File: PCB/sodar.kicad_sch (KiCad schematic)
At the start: 70 parts, among them J1 Screw_Terminal_01x02, J2 Conn_02x12_Counter_Clockwise, J3 Conn_01x02, U1 TC78H621FNG, U10 TC78H621FNG, U2 TC78H621FNG, U3 TC78H621FNG, U4 TC78H621FNG, U5 TC78H621FNG, U6 TC78H621FNG, U7 TC78H621FNG, U8 TC78H621FNG, U9 TC78H621FNG

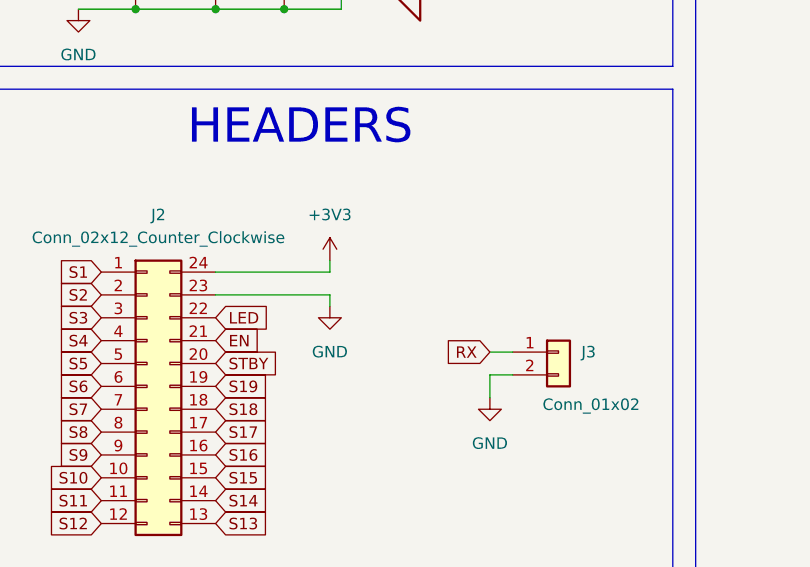
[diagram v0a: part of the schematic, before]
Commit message: Added a bulk cap on 3V3 line
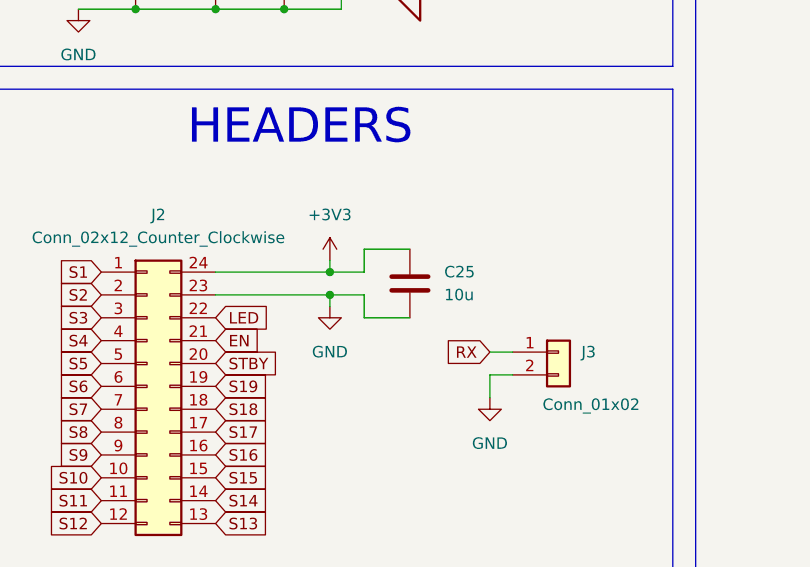
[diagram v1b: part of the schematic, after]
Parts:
- added C25: 10u, Capacitor_SMD:C_0805_2012Metric, symbol Device:C
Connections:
- net +3V3: now also C25.1
- net GND: now also C25.2
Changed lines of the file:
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@@
 	)
 	(junction
+		(at 217.17 66.04)
+		(diameter 0)
+		(color 0 0 0 0)
+	)
+	(junction
 		(at 347.98 76.2)
 		(diameter 0)
@@
 	)
 	(junction
+		(at 217.17 63.5)
+		(diameter 0)
+		(color 0 0 0 0)
+	)
+	(junction
 		(at 140.97 138.43)
 		(diameter 0)
@@
 	(wire
 		(pts
+			(xy 220.98 68.58) (xy 226.06 68.58)
+		)
+		(stroke
+			(width 0)
+			(type default)
+		)
+	)
+	(wire
+		(pts
 			(xy 104.14 66.04) (xy 104.14 67.31)
 		)
@@
 	(wire
 		(pts
+			(xy 220.98 63.5) (xy 217.17 63.5)
+		)
+		(stroke
+			(width 0)
+			(type default)
+		)
+	)
+	(wire
+		(pts
 			(xy 130.81 147.32) (xy 135.89 147.32)
 		)
@@
 	(wire
 		(pts
+			(xy 220.98 60.96) (xy 220.98 63.5)
+		)
+		(stroke
+			(width 0)
+			(type default)
+		)
+	)
+	(wire
+		(pts
 			(xy 29.21 175.26) (xy 30.48 175.26)
 		)
@@
 	(wire
 		(pts
+			(xy 220.98 66.04) (xy 220.98 68.58)
+		)
+		(stroke
+			(width 0)
+			(type default)
+		)
+	)
+	(wire
+		(pts
 			(xy 140.97 96.52) (xy 140.97 104.14)
 		)
@@
 	(wire
 		(pts
+			(xy 226.06 60.96) (xy 220.98 60.96)
+		)
+		(stroke
+			(width 0)
+			(type default)
+		)
+	)
+	(wire
+		(pts
 			(xy 240.03 124.46) (xy 240.03 121.92)
 		)
@@
 	(wire
 		(pts
+			(xy 217.17 66.04) (xy 220.98 66.04)
+		)
+		(stroke
+			(width 0)
+			(type default)
+		)
+	)
+	(wire
+		(pts
 			(xy 285.75 41.91) (xy 285.75 45.72)
 		)
@@
 					(unit 1)
 				)
+			)
+		)
+	)
+	(symbol
+		(lib_id "Device:C")
+		(at 226.06 64.77 0)
+		(unit 1)
+		(exclude_from_sim no)
+		(in_bom yes)
+		(on_board yes)
+		(dnp no)
+		(fields_autoplaced yes)
+		(property "Reference" "C25"
+			(at 229.87 63.4999 0)
+			(effects
+				(font
+					(size 1.27 1.27)
+				)
+				(justify left)
+			)
+		)
+		(property "Value" "10u"
+			(at 229.87 66.0399 0)
+			(effects
+				(font
+					(size 1.27 1.27)
+				)
+				(justify left)
+			)
+		)
+		(property "Footprint" "Capacitor_SMD:C_0805_2012Metric"
+			(at 227.0252 68.58 0)
+			(effects
+				(font
+					(size 1.27 1.27)
+				)
+				(hide yes)
+			)
+		)
+		(property "Datasheet" "~"
+			(at 226.06 64.77 0)
+			(effects
+				(font
+					(size 1.27 1.27)
+				)
+				(hide yes)
+			)
+		)
+		(property "Description" "Unpolarized capacitor"
+			(at 226.06 64.77 0)
+			(effects
+				(font
+					(size 1.27 1.27)
+				)
+				(hide yes)
+			)
+		)
+		(pin "2"
+		)
+		(pin "1"
+		)
+		(instances
+			(project ""
+				(path "/f620949f-55f1-4ffa-a6f4-2a6276be8919"
+					(reference "C25")
+					(unit 1)
+				)

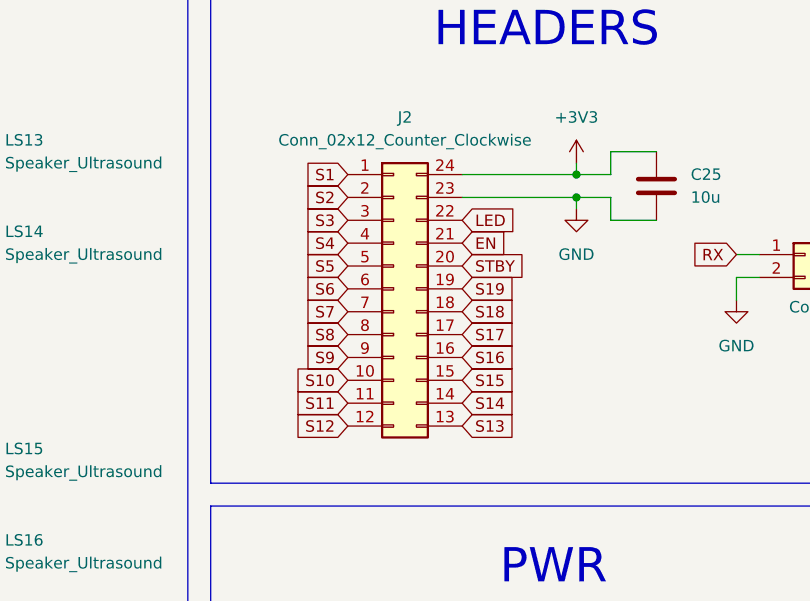
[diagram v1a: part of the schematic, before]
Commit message: Moved signal connections on the header for easier routing
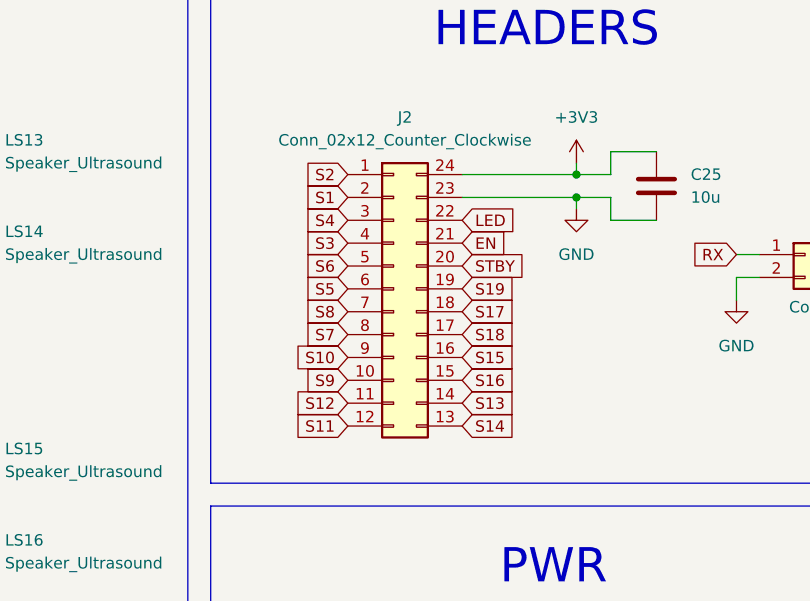
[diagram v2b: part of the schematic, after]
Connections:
- net S1: now also J2.2 (Pin_2); no longer J2.1 (Pin_1)
- net S10: now also J2.9 (Pin_9); no longer J2.10 (Pin_10)
- net S11: now also J2.12 (Pin_12); no longer J2.11 (Pin_11)
- net S12: now also J2.11 (Pin_11); no longer J2.12 (Pin_12)
- net S13: now also J2.14 (Pin_14); no longer J2.13 (Pin_13)
- net S14: now also J2.13 (Pin_13); no longer J2.14 (Pin_14)
- net S15: now also J2.16 (Pin_16); no longer J2.15 (Pin_15)
- net S16: now also J2.15 (Pin_15); no longer J2.16 (Pin_16)
- net S17: now also J2.18 (Pin_18); no longer J2.17 (Pin_17)
- net S18: now also J2.17 (Pin_17); no longer J2.18 (Pin_18)
- net S2: now also J2.1 (Pin_1); no longer J2.2 (Pin_2)
- net S3: now also J2.4 (Pin_4); no longer J2.3 (Pin_3)
- net S4: now also J2.3 (Pin_3); no longer J2.4 (Pin_4)
- net S5: now also J2.6 (Pin_6); no longer J2.5 (Pin_5)
- net S6: now also J2.5 (Pin_5); no longer J2.6 (Pin_6)
- net S7: now also J2.8 (Pin_8); no longer J2.7 (Pin_7)
- net S8: now also J2.7 (Pin_7); no longer J2.8 (Pin_8)
- net S9: now also J2.10 (Pin_10); no longer J2.9 (Pin_9)

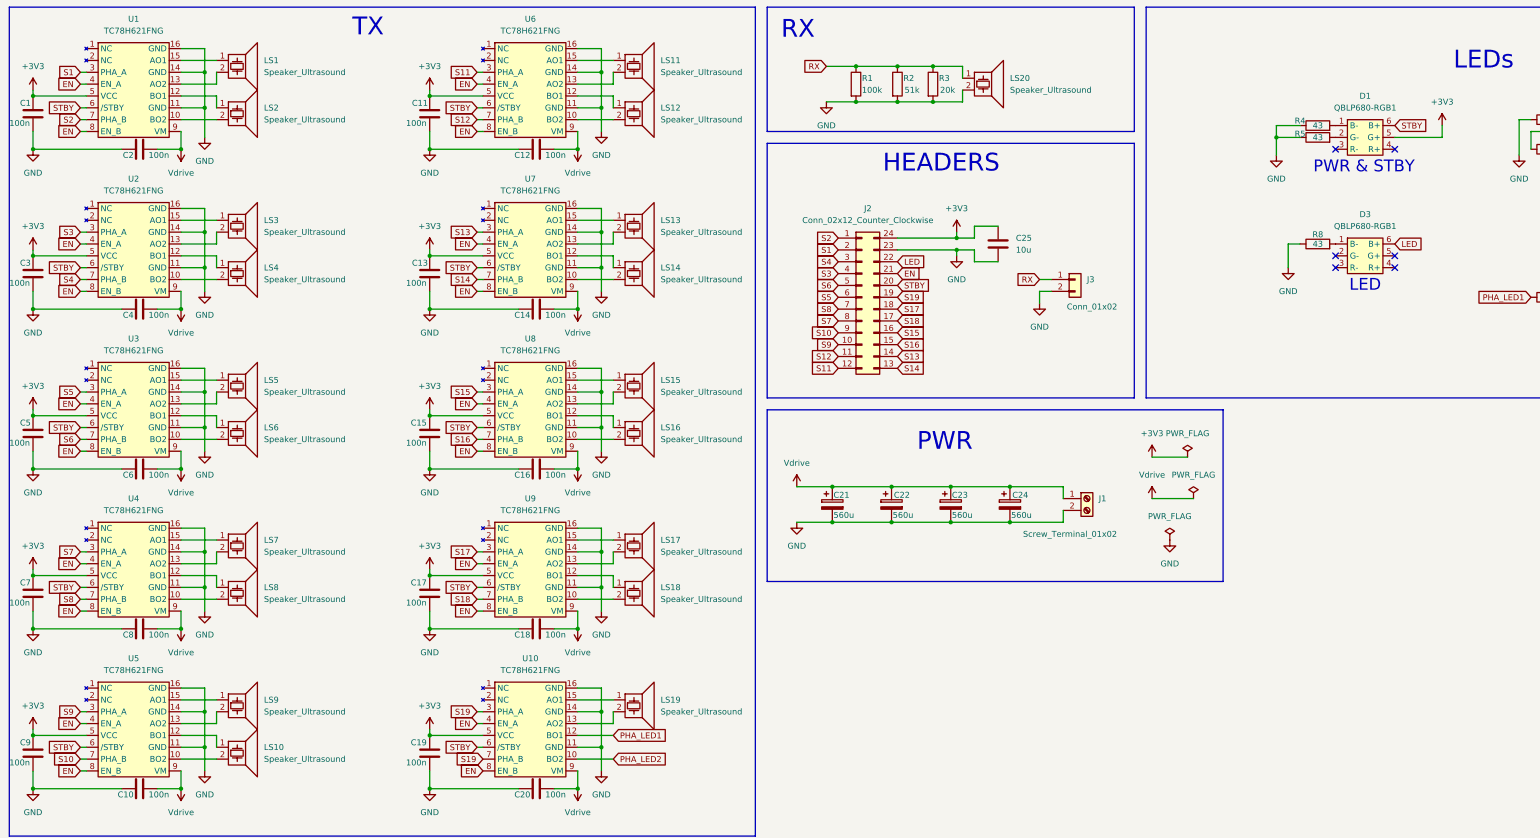
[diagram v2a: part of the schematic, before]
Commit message: Rerouted STBY to 3V3 as we set it to 3V3 anyway
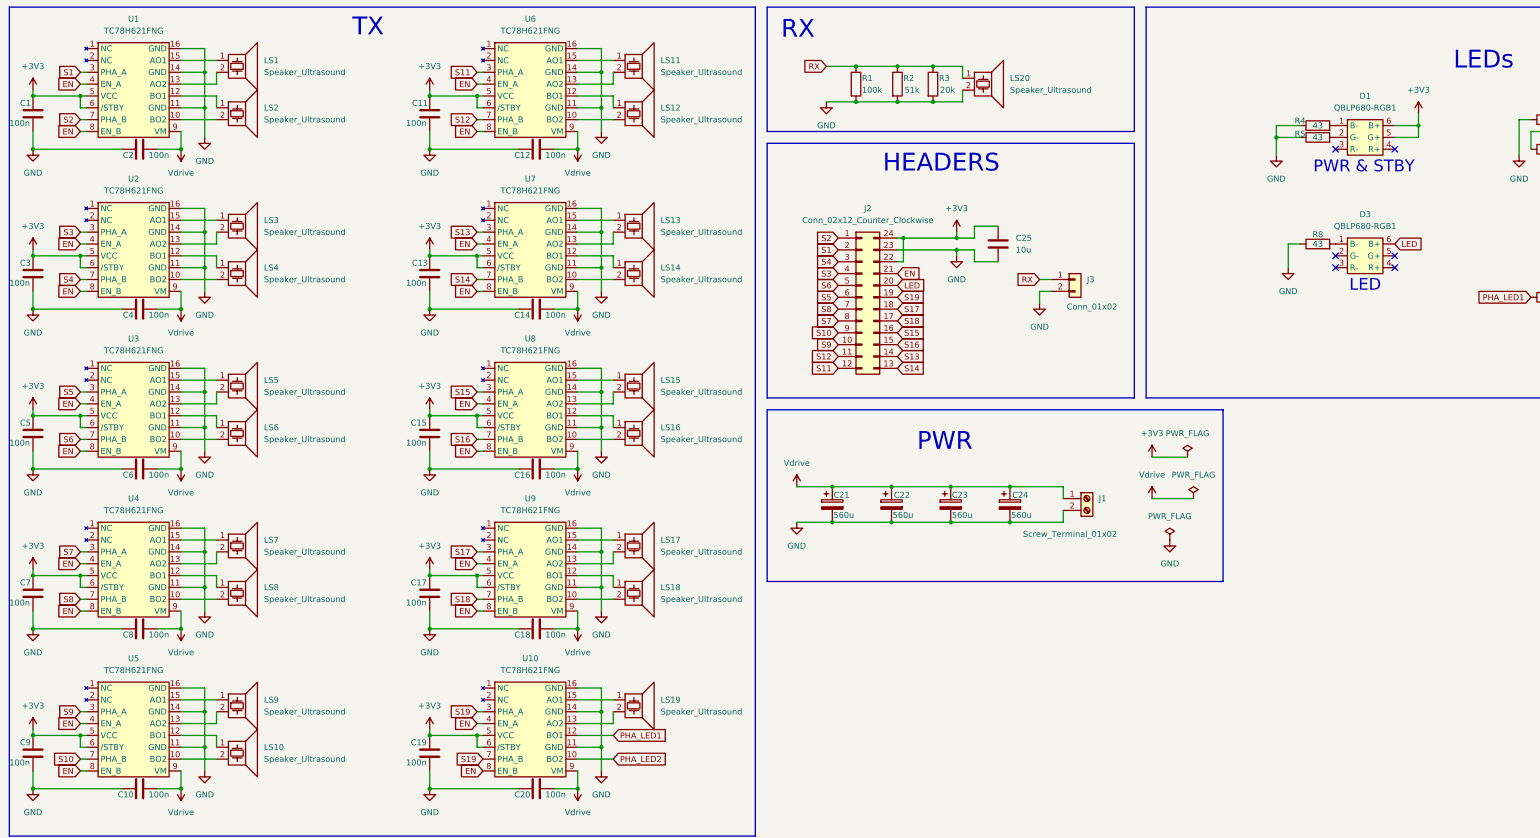
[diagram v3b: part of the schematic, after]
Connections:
- net +3V3: now also D1.6 (B+), J2.22 (Pin_22), U1.6 (/STBY), U10.6 (/STBY), U2.6 (/STBY), U3.6 (/STBY), U4.6 (/STBY), U5.6 (/STBY), U6.6 (/STBY), U7.6 (/STBY), U8.6 (/STBY), U9.6 (/STBY)
- net LED: now also J2.20 (Pin_20); no longer J2.22 (Pin_22)
- removed net STBY: D1.6 (B+), J2.20 (Pin_20), U1.6 (/STBY), U10.6 (/STBY), U2.6 (/STBY), U3.6 (/STBY), U4.6 (/STBY), U5.6 (/STBY), U6.6 (/STBY), U7.6 (/STBY), U8.6 (/STBY), U9.6 (/STBY)
